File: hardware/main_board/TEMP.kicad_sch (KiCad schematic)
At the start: 21 parts, among them IC2 LP2950-33LPRE3, J1 Header2, J3 Conn_01x06_Pin, SW2 UP, U3 M0G3507QDGS32RQ1

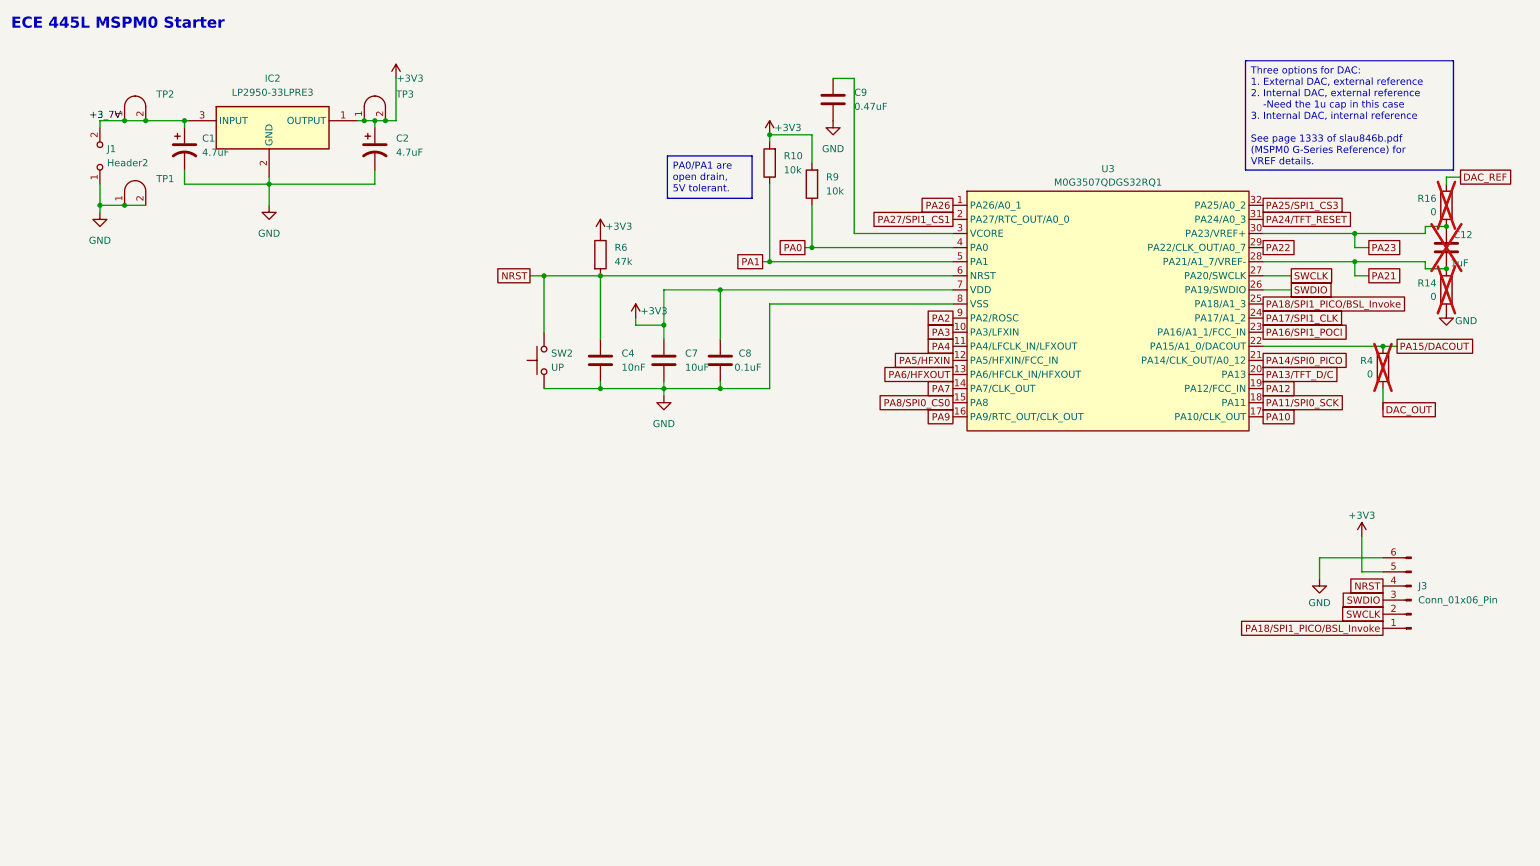
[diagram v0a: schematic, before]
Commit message: replaced LDO thing to be free one in lab checkout. added some stuff to main board (wip)
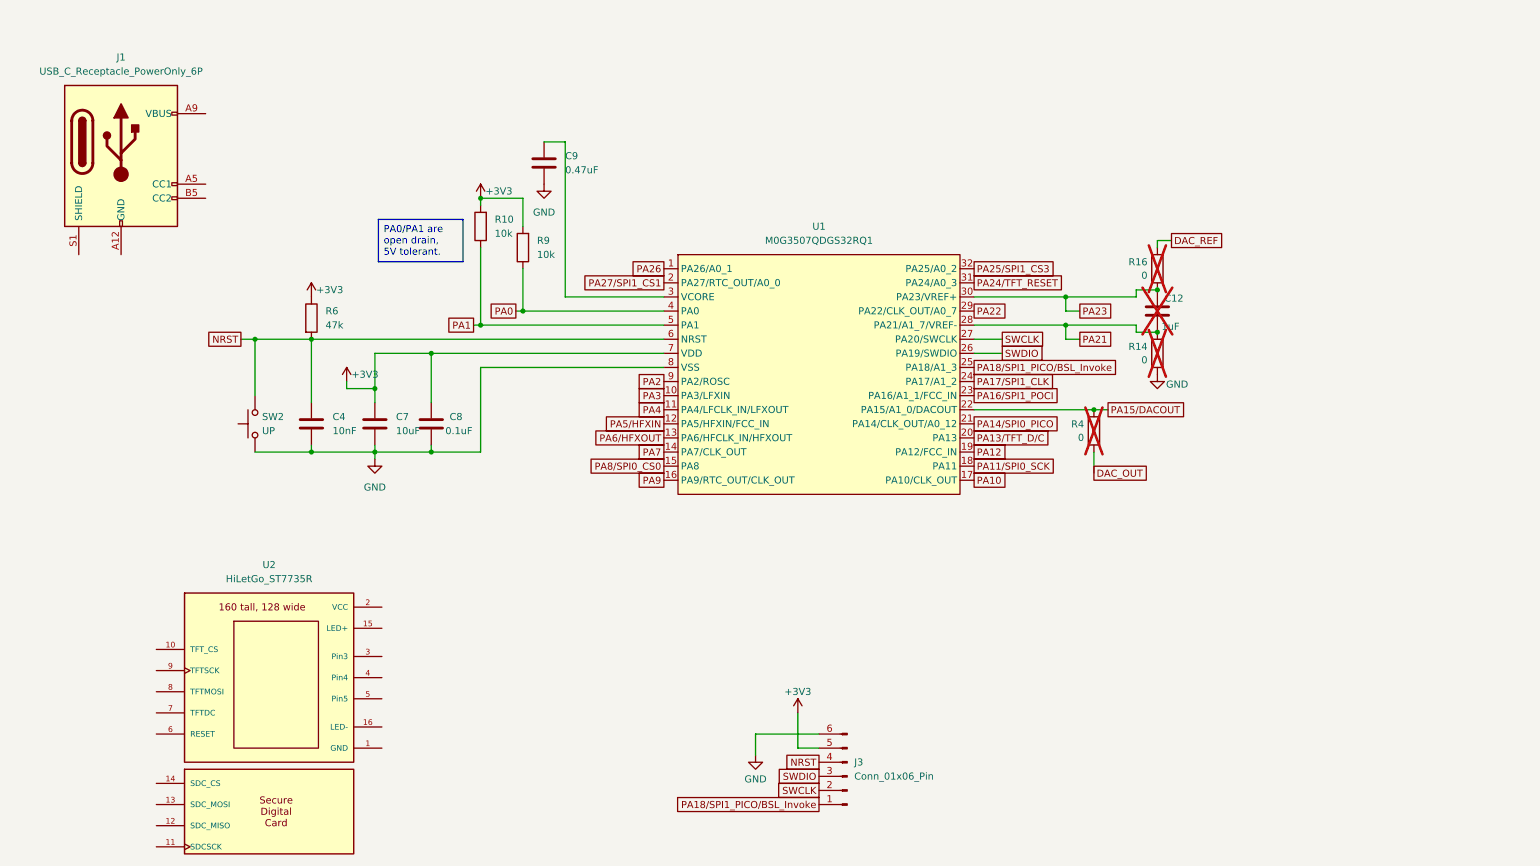
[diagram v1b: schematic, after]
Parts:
- removed C1, C2: 4.7uF, ECE445L:CP_Radial_Tantal200mil, symbol ECE445L:C_Polarized
- removed IC2: LP2950-33LPRE3, Package_TO_SOT_THT:TO-92_Inline_Wide, symbol ECE445L:LP2950-33LPRE3
- removed J1: Header2, ECE445L:PinHeader_1x02_P2.54mm_Vertical, symbol ECE445L:Battery_Header
- removed TP1, TP2, TP3: TP, ECE445L:Testpoint_1x02_P2.54mm, symbol ECE445L:Testpoint
- removed U3: M0G3507QDGS32RQ1, 445L:generic_VSSOP_0.5mm, symbol ECE445L:M0G3507QDGS32RQ1
- added J1: USB_C_Receptacle_PowerOnly_6P, symbol Connector:USB_C_Receptacle_PowerOnly_6P
- added U1: M0G3507QDGS32RQ1, 445L:generic_VSSOP_0.5mm, symbol ECE445L:M0G3507QDGS32RQ1
- added U2: HiLetGo_ST7735R, 445L:hiletgo_st7735r, symbol ECE445L:HiLetGo_ST7735R
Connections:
- net +3V3: now also U1.7 (VDD)
- net GND: now also U1.8 (VSS)
- net NRST: now also U1.6 (NRST)
- net PA0: now also U1.4 (PA0)
- net PA1: now also U1.5 (PA1)
- net PA10: now also U1.17 (PA10/CLK_OUT)
- net PA11/SPI0_SCK: now also U1.18 (PA11)
- net PA12: now also U1.19 (PA12/FCC_IN)
- net PA13/TFT_D/C: now also U1.20 (PA13)
- net PA14/SPI0_PICO: now also U1.21 (PA14/CLK_OUT/A0_12)
- net PA15/DACOUT: now also U1.22 (PA15/A1_0/DACOUT)
- net PA16/SPI1_POCI: now also U1.23 (PA16/A1_1/FCC_IN)
- net PA17/SPI1_CLK: now also U1.24 (PA17/A1_2)
- net PA18/SPI1_PICO/BSL_Invoke: now also U1.25 (PA18/A1_3)
- net PA2: now also U1.9 (PA2/ROSC)
- net PA21: now also U1.28 (PA21/A1_7/VREF-)
- net PA22: now also U1.29 (PA22/CLK_OUT/A0_7)
- net PA23: now also U1.30 (PA23/VREF+)
- net PA24/TFT_RESET: now also U1.31 (PA24/A0_3)
- net PA25/SPI1_CS3: now also U1.32 (PA25/A0_2)
- net PA26: now also U1.1 (PA26/A0_1)
- net PA27/SPI1_CS1: now also U1.2 (PA27/RTC_OUT/A0_0)
- net PA3: now also U1.10 (PA3/LFXIN)
- net PA4: now also U1.11 (PA4/LFCLK_IN/LFXOUT)
- net PA5/HFXIN: now also U1.12 (PA5/HFXIN/FCC_IN)
- net PA6/HFXOUT: now also U1.13 (PA6/HFCLK_IN/HFXOUT)
- net PA7: now also U1.14 (PA7/CLK_OUT)
- net PA8/SPI0_CS0: now also U1.15 (PA8)
- net PA9: now also U1.16 (PA9/RTC_OUT/CLK_OUT)
- net SWCLK: now also U1.27 (PA20/SWCLK)
- net SWDIO: now also U1.26 (PA19/SWDIO)
- net at C9.1: now also U1.3 (VCORE)
- new net: J1.A12 (GND), J1.B12 (GND)
- new net: J1.A9 (VBUS), J1.B9 (VBUS)
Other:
- note removed: "ECE 445L MSPM0 Starter"
- company: The University of Texas at Austin -> (none)
- title: ECE 445L Lab6 Project -> (none)
- moved on the sheet: C12, C4, C7, C8, C9, J3, R10, R14, R16, R4, R6, R9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
